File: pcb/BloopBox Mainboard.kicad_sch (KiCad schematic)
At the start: 34 parts, among them J2 SPKR, J3 Raspberry_Pi, J4 I2C, J5 NFC-Module, J6 GPIO, J7 TailBoard, J8 PROG, Q5 2N7002, Q6 2N7002, U1 MAX98357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

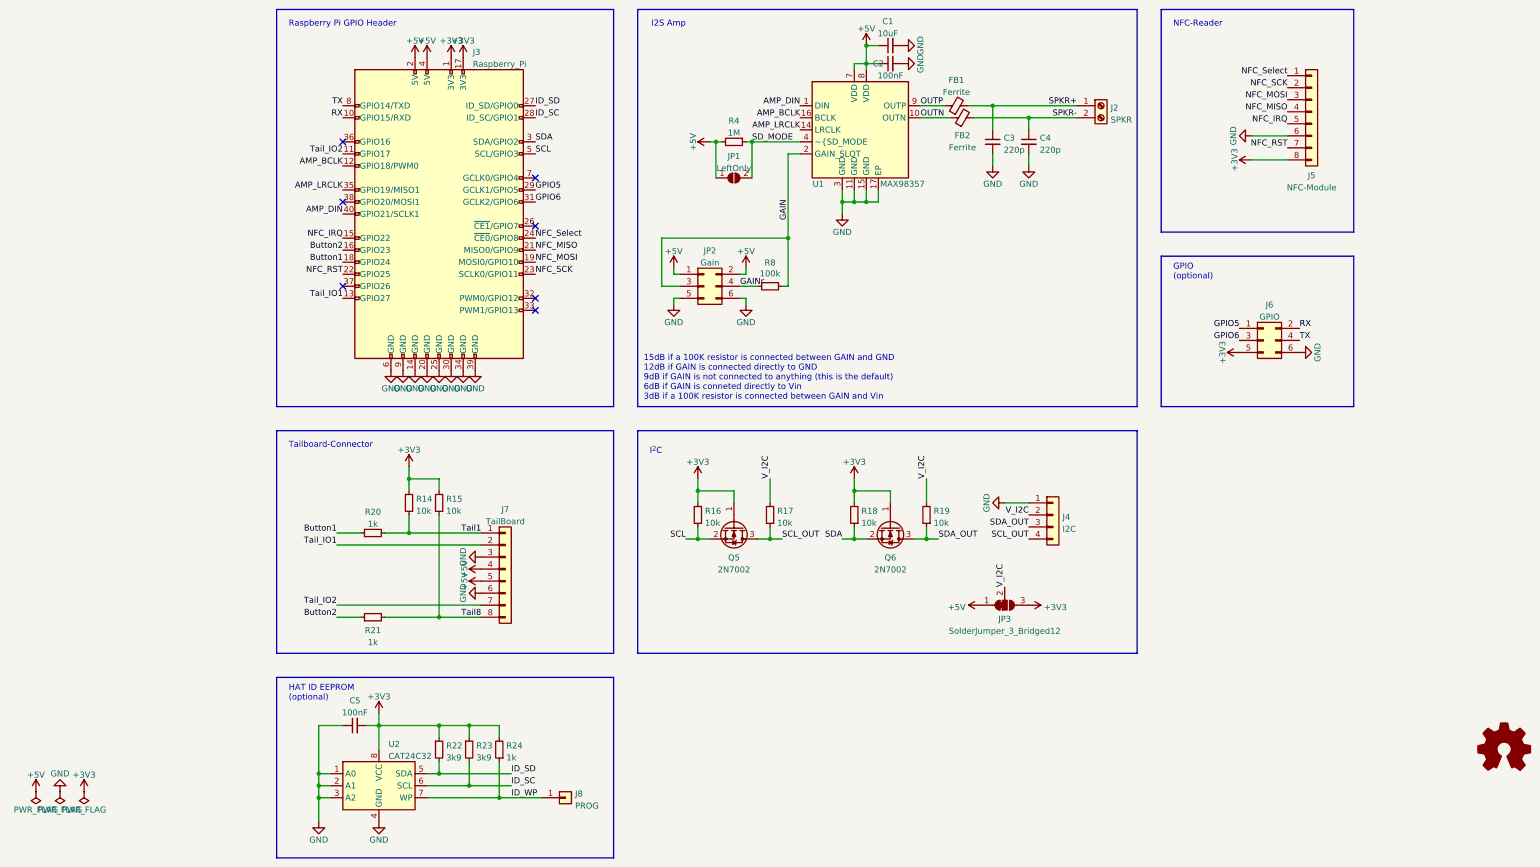
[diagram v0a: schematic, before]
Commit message: feat!: remove I2C level shifter
The new LED driver needs 3.3V I2C anyway so the level shifter is not needed anymore.
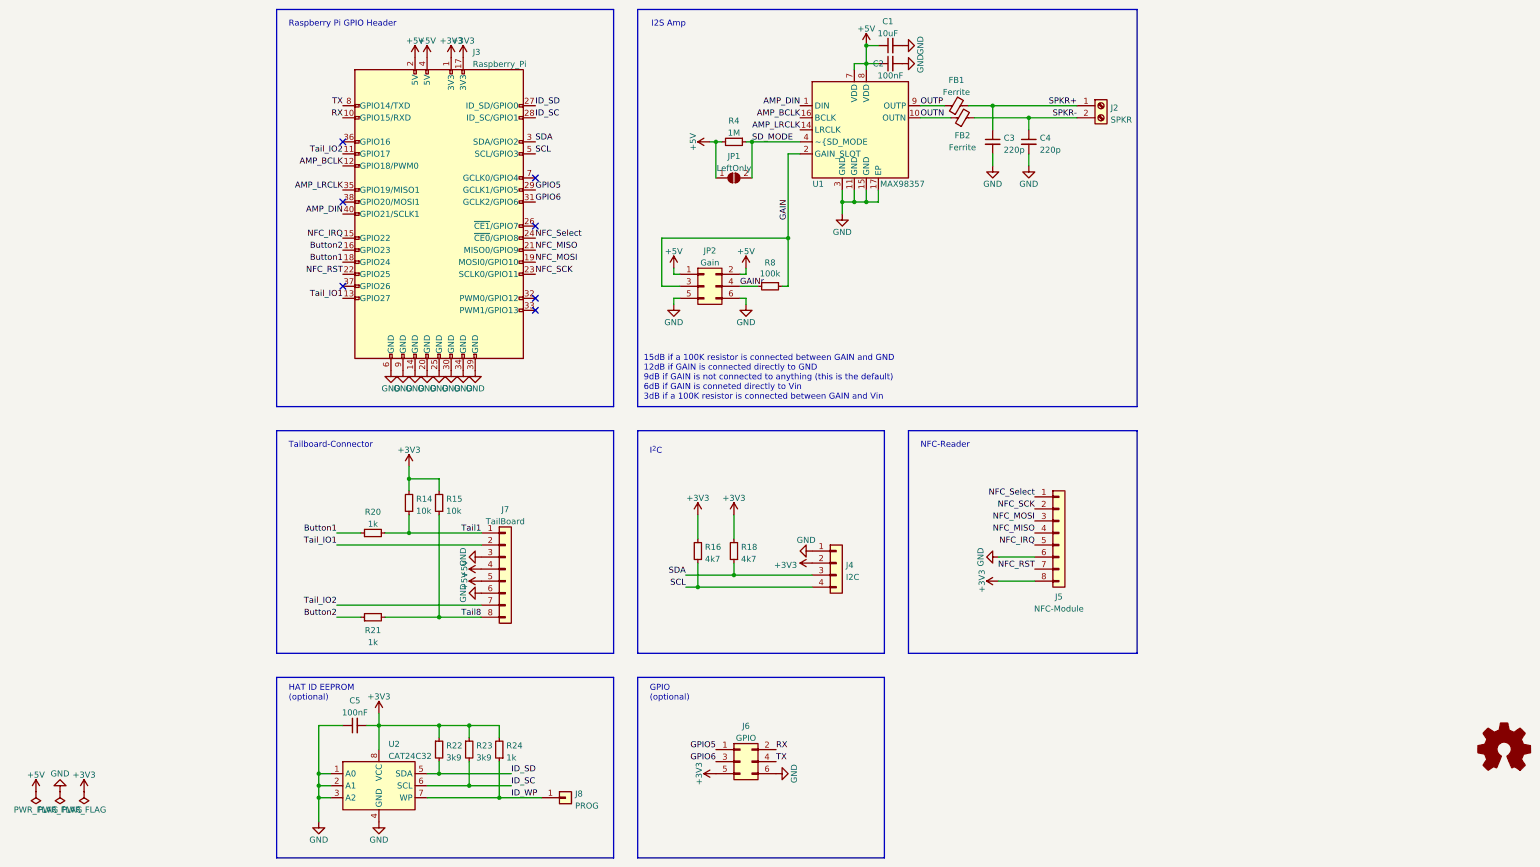
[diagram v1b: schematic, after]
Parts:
- removed JP3: SolderJumper_3_Bridged12, Jumper:SolderJumper-3_P1.3mm_Bridged12_RoundedPad1.0x1.5mm, symbol Jumper:SolderJumper_3_Bridged12
- removed Q5, Q6: 2N7002, Package_TO_SOT_SMD:SOT-23, symbol Transistor_FET:2N7002
- removed R17, R19: 10k, Resistor_SMD:R_0402_1005Metric, symbol Device:R_Small
- R16, R18: value 10k -> 4k7
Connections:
- net SCL_OUT is gone; now on net SCL: J4.4 (Pin_4)
- net SDA_OUT is gone; now on net SDA: J4.3 (Pin_3)
- net V_I2C is gone; now on net +3V3: J4.2 (Pin_2)
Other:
- moved on the sheet: J4, J5, J6, R16, R18

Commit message: feat!: remove HAT EEPROM
Since it is more effort to program each EEPROM after assembly than manually changing the settings it could handle, the EEPROM would only be a novelty and was removed.
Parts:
- removed C5: 100nF, Capacitor_SMD:C_0402_1005Metric, symbol Device:C_Small
- removed J8: PROG, TestPoint:TestPoint_THTPad_1.0x1.0mm_Drill0.5mm, symbol Connector_Generic:Conn_01x01
- removed R22, R23: 3k9, Resistor_SMD:R_0402_1005Metric, symbol Device:R_Small
- removed R24: 1k, Resistor_SMD:R_0402_1005Metric, symbol Device:R_Small
- removed U2: CAT24C32, Package_DFN_QFN:DFN-8-1EP_3x2mm_P0.5mm_EP1.3x1.5mm, symbol Memory_EEPROM:CAT24C128
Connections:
- net ID_SC: no longer names the net of J3.28 (ID_SC/GPIO1)
- net ID_SD: no longer names the net of J3.27 (ID_SD/GPIO0)
- no-connect marks 7 -> 9
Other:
- note added: "GPIO & UART"
- note added: "I^{2}C for LED-Board"
- note removed: "GPIO (optional)"
- note removed: "HAT ID EEPROM (optional)"
- note removed: "I^{2}C"
- moved on the sheet: J6

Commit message: fix: change LCSC part number of I2C pullup
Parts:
- R16, R18: LCSC C25744 -> C25900
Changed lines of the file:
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@@
       (effects (font (size 1.27 1.27)) hide)
     )
-    (property "LCSC" "C25744" (id 4) (at 115.57 132.08 0)
+    (property "LCSC" "C25900" (id 4) (at 115.57 132.08 0)
       (effects (font (size 1.27 1.27)) hide)
     )
@@
       (effects (font (size 1.27 1.27)) hide)
     )
-    (property "LCSC" "C25744" (id 4) (at 107.95 132.08 0)
-      (effects (font (size 1.27 1.27)) hide)
-    )
+    (property "LCSC" "C25900" (id 4) (at 107.95 132.08 0)
+      (effects (font (size 1.27 1.27)) hide)
+    )

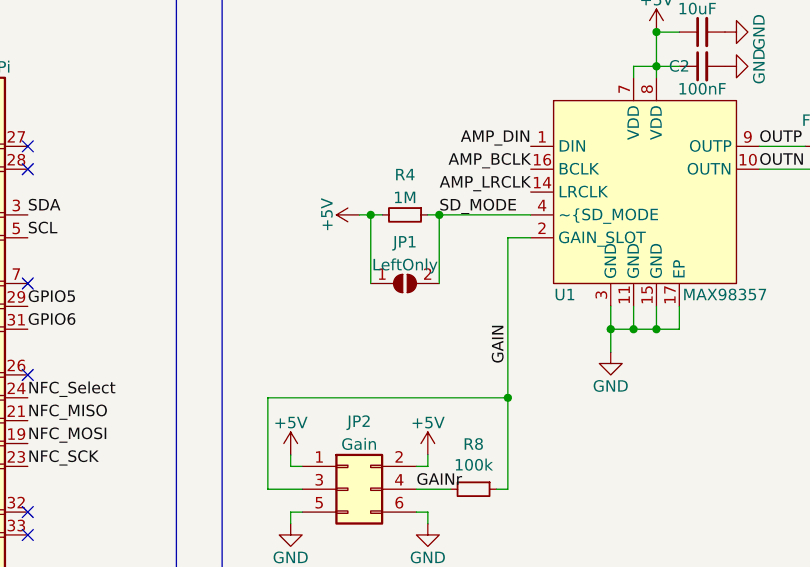
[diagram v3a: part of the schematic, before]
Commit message: chore: update to KiCad 7
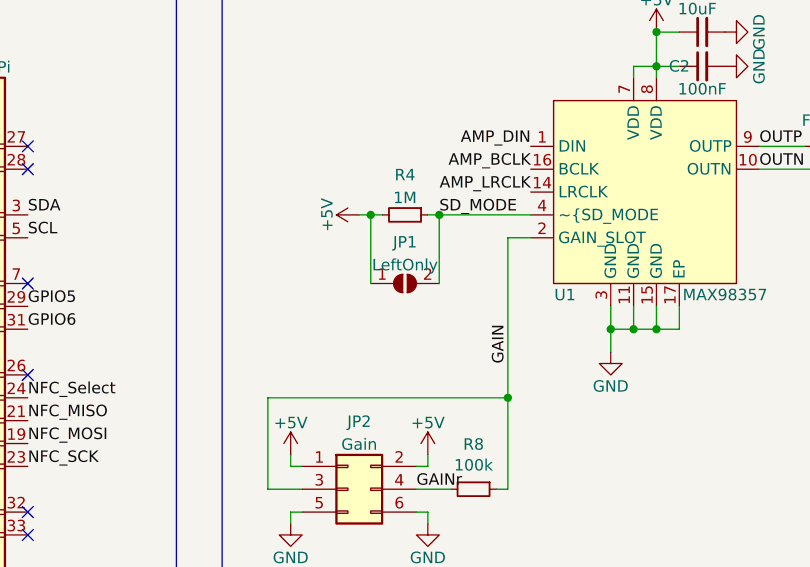
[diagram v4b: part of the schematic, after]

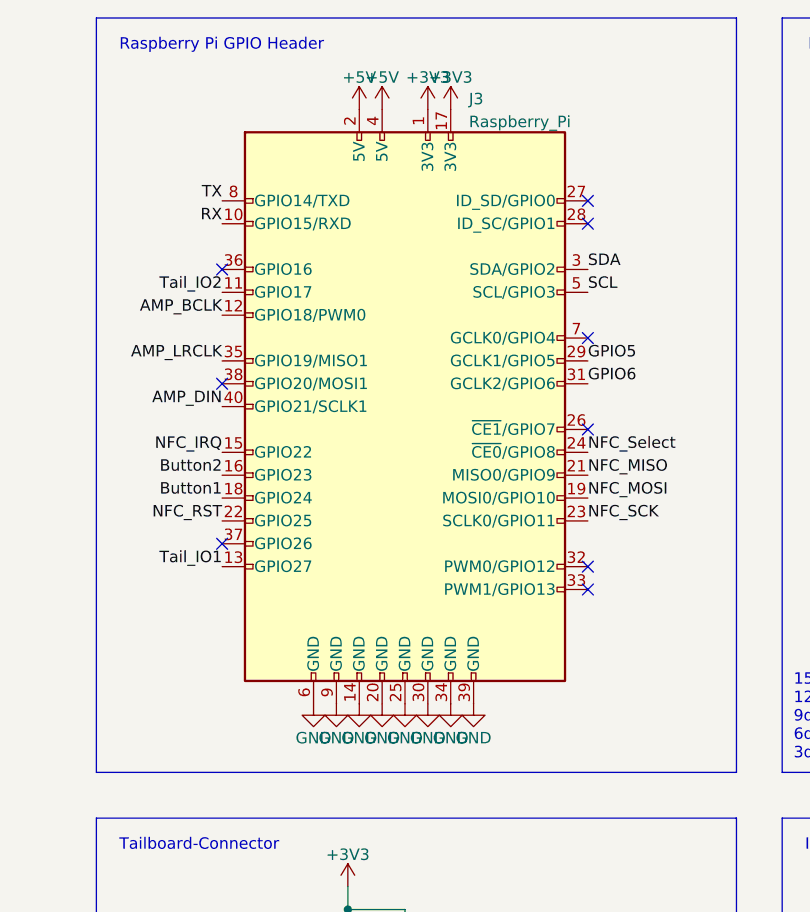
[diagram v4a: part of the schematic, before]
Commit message: chore: update to KiCad 8
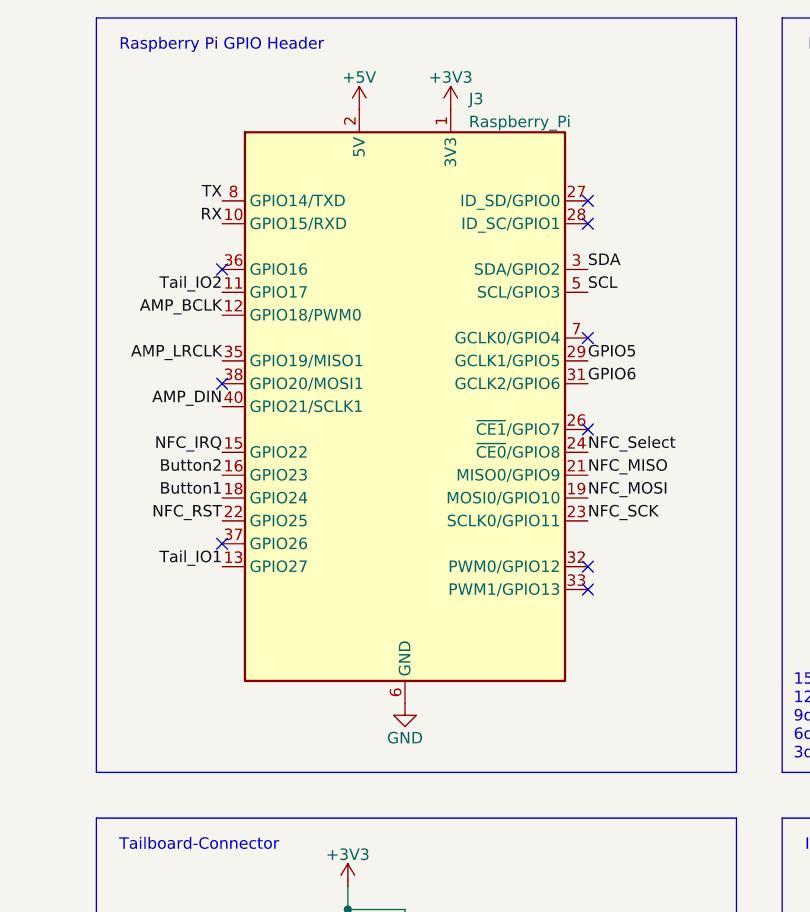
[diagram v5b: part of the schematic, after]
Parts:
- J2: LCSC C722769 -> C49992
- J4: LCSC C722777 -> C49994
- J5, J7: LCSC C722793 -> C20598766
